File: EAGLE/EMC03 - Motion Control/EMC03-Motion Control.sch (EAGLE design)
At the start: 255 parts, among them J1 UART0, J10 S4B-PH-SM4, J11 S4B-PH-SM4, J12 S4B-PH-SM4, J13 S5B-PH-SM4, J14 S5B-PH-SM4, J15 S5B-PH-SM4, J16 S8B-PH-SM4, J17 S8B-PH-SM4, J18 S6B-PH-SM4, J19 S6B-PH-SM4, J2 FTSH-105-1-L-DV, J20 Intel EDISON, J21 PWRBUTTON, J22 SERIAL CONS., J23 B14B-PH, J3 USB-A, J4 101-00581-59, J5 S3B-PH-SM4, J6 S3B-PH-SM4, J7 S3B-PH-SM4, J8 694106106102, J9 ESTOP, Q1 12MHz, Q2 25MHz, U1 LPC1768, U10 FT231XS-R, U11 74LVC1T45, U12 74LVC1T45, U13 74LVC1T45, U14 74LVC1T45, U15 74LVC1T45, U16 TXS0206-29, U17 74LVC, U18 MIC2026-1YM, U19 MIC2026-1YM, U2 SP3485, U20 74LVC, U21 74LVC1T45, U22 74LVC1T45, U3 93LC66A, U4 LAN9514, U5 74AHCT, U6 TMC2130-LA, U7 TMC2130-LA, U8 TMC2130-LA, U9 SP3485

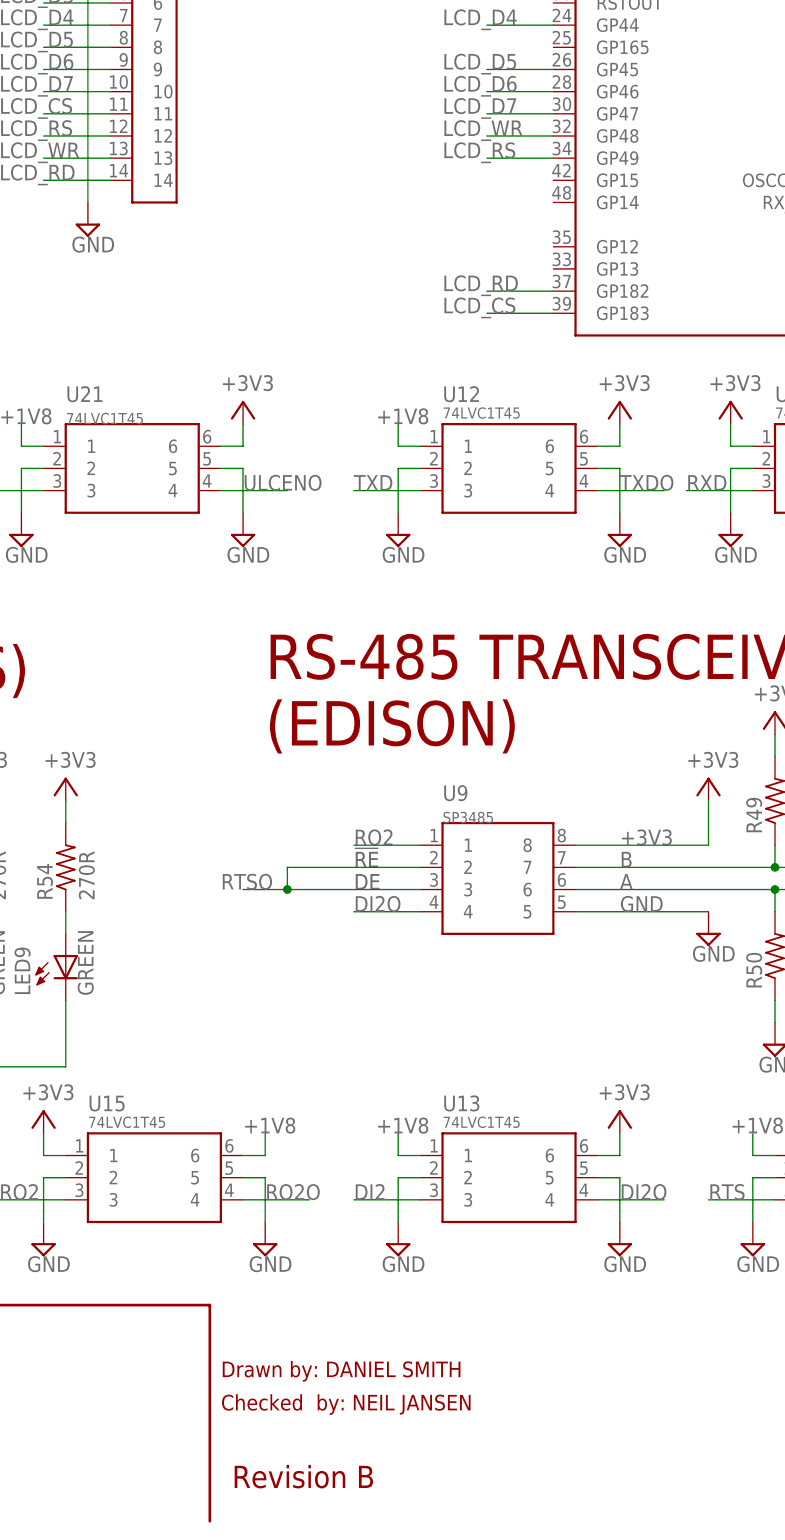
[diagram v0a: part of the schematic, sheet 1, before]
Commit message: Preliminary placement and routing done for EFD01. Preliminary placement done for EMC03. All schematics are ready for review (A0 for ECAM03 needs to be defined, also SS for EFD01, ECAM03, etc.)
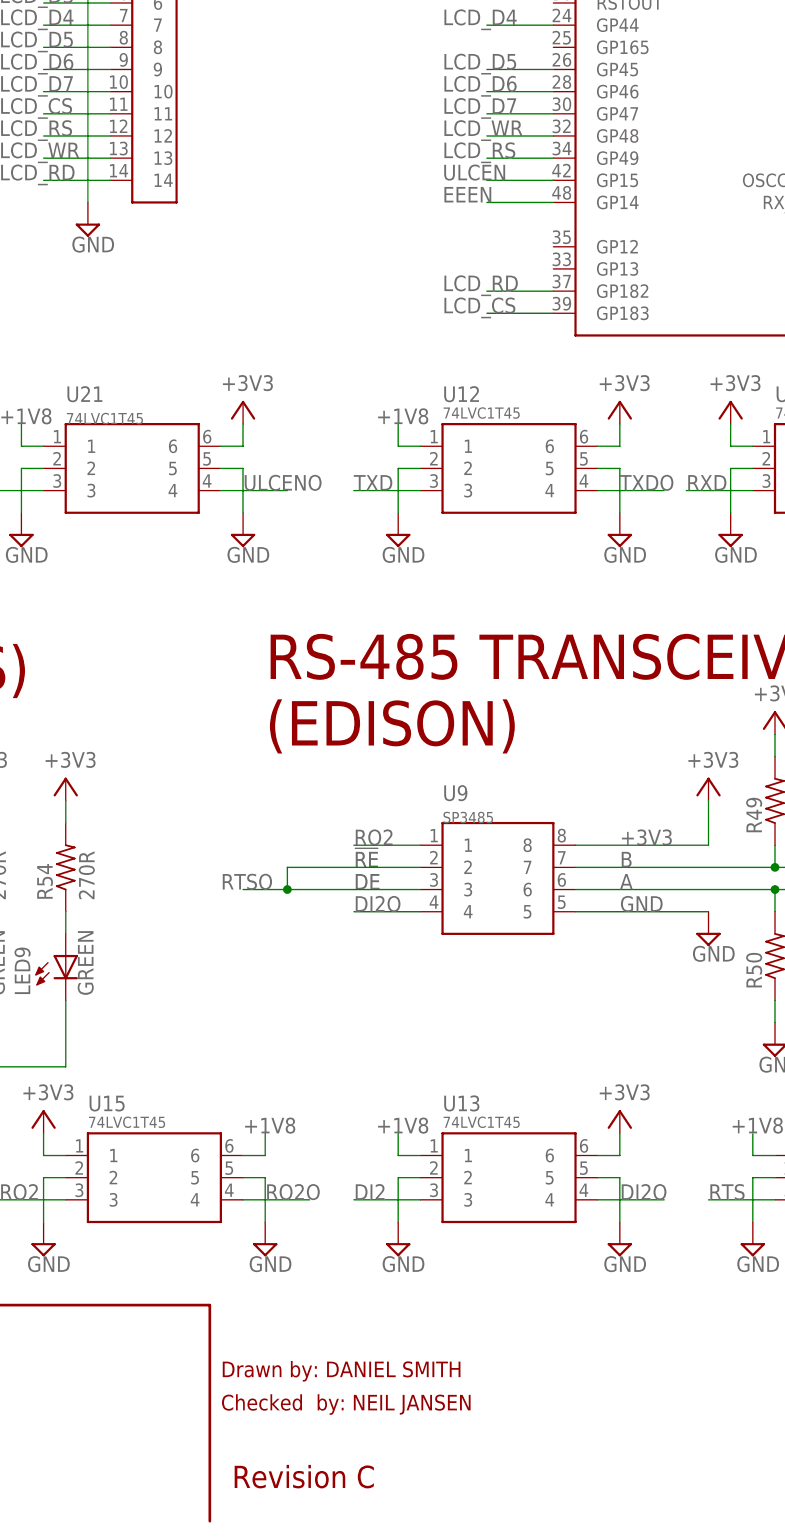
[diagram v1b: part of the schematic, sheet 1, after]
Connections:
- net EEEN: now also J20.GP14
- net ULCEN: now also J20.GP15
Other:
- note added: "Revision C"
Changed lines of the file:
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@@
 <text x="289.56" y="20.32" size="1.778" layer="94" ratio="15">Drawn by: DANIEL SMITH</text>
 <text x="289.56" y="16.51" size="1.778" layer="94" ratio="15">Checked  by: NEIL JANSEN</text>
-<text x="290.83" y="7.62" size="2.54" layer="94" ratio="10">Revision B</text>
+<text x="290.83" y="7.62" size="2.54" layer="94" ratio="10">Revision C</text>
 <wire x1="5.715" y1="28.575" x2="288.29" y2="28.575" width="0.3048" layer="94"/>
 <wire x1="288.29" y1="28.575" x2="288.29" y2="3.81" width="0.3048" layer="94"/>
@@
 <label x="256.54" y="121.92" size="1.778" layer="95"/>
 </segment>
+<segment>
+<pinref part="J20" gate="G$1" pin="GP15"/>
+<wire x1="327.66" y1="157.48" x2="320.04" y2="157.48" width="0.1524" layer="91"/>
+<label x="314.96" y="157.48" size="1.778" layer="95"/>
+</segment>
 </net>
 <net name="EEENO" class="0">
@@
 <label x="210.82" y="121.92" size="1.778" layer="95"/>
 </segment>
-</net>
+<segment>
+<pinref part="J20" gate="G$1" pin="GP14"/>
+<wire x1="327.66" y1="154.94" x2="320.04" y2="154.94" width="0.1524" layer="91"/>
+<label x="314.96" y="154.94" size="1.778" layer="95"/>
+</segment>
+</net>

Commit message: Split the EMC03 into EMC03 and EFP01 (front panel board) to make routing 10000000x easier
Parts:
- removed C13, C14, C18, C19, C20, C21, C22, C23, C33, C34, C35, C60, C74, C79, C80, C81, C82, C84, C85: 0.1uF, TinWhiskers:CPL-CAP-X5R-0603-0.1UF-35V
- removed C24, C25, C77: 0.1uF, TinWhiskers:CPL-CAP-X7R-0603-0.1UF-35V
- removed C26, C30, C31, C32: 18pF, TinWhiskers:CPL-CAP-C0G-0603-18PF-50V
- removed C3: 100uF, rcl:CPOL-USD
- removed C37: 220uF, TinWhiskers:CPL-CAP-ALU-SMD-220-50V
- removed C38: 470uF, TinWhiskers:CPL-CAP-ALU-SMD-470UF-25V
- removed C4: 0.1uF, TinWhiskers:CPL-CAP-X7R-0603-100NF-50V
- removed C61, C83: 4.7uF, TinWhiskers:CPL-CAP-X5R-0603-4.7UF-10V
- removed C73: 1.0uF, TinWhiskers:CPL-CAP-X5R-0603-1UF-50V
- removed C76: 0.47uF, TinWhiskers:CPL-CAP-X7R-0603-0.47UF-10V
- removed C78: 10nF, TinWhiskers:CPL-CAP-X7R-10NF-16V
- removed D2: SJPB-H6, TinWhiskers:CPL-DIO-SJPB-H6-SM2
- removed FB1, FB3, FB4: 120R, TinWhiskers:CPL-IND-FER-120OHM-2A
- removed FID1, FID2, FID3, FID4, FID5, FID6, FID7: FIDUCIAL, FirePick:FIDUCIAL
- removed J20: Intel EDISON, TinWhiskers:CPL-SBC-INTEL-EDISON
- removed J21: PWRBUTTON, TinWhiskers:CPL-CON-HEADER-0.1IN-2P-M
- removed J22: SERIAL CONS., TinWhiskers:CPL-CON-HEADER-0.1IN-4P-M
- removed J23: B14B-PH, TinWhiskers:CPL-CON-JST-2.0MM-14P-M-VRT
- removed J8: 694106106102, TinWhiskers:CPL-CON-BARREL-2.1MM-24V
- removed L1: 100uH, TinWhiskers:CPL-IND-100UH-1.8A
- removed LED10, LED11, LED12, LED13, LED14, LED8, LED9: GREEN, TinWhiskers:CPL-LED-0603-GREEN
- removed LED6, LED7: RED, TinWhiskers:CPL-LED-0603-RED
- removed LOGO4: LOGO-FIREPICKLARGE, FirePick:LOGO-FIREPICKLARGE
- removed LOGO5: LOGO-OSHWMEDIUM, FirePick:LOGO-OSHWMEDIUM
- removed LOGO6: LOGO-CC-BY-SALARGE, FirePick:LOGO-CC-BY-SALARGE
- removed Q2: 25MHz, TinWhiskers:CPL-OSC-CRY-25MHZ-18PF
- removed R11: 1M, TinWhiskers:CPL-RES-0603-1M-0.1W
- removed R12: 825R, TinWhiskers:CPL-RES-0603-825-0.1W
- removed R13: 12.4K, TinWhiskers:CPL-RES-0603-12.4K-0.1W
- removed R14, R43, R48: 10K, TinWhiskers:CPL-RES-0603-10K-0.1W
- removed R15, R57: 0R1, TinWhiskers:CPL-RES-0603-0.1-0.1W
- removed R16, R58: DNP, TinWhiskers:CPL-RES-0603-0-0.1W
- removed R17, R23: 10.5K, TinWhiskers:CPL-RES-0603-10.5K-0.1W
- removed R22, R30, R31, R32: 49R9, TinWhiskers:CPL-RES-0603-49.9-0.1W
- removed R33, R34: 330R, TinWhiskers:CPL-RES-0603-330-0.1W
- removed R35: 12K, TinWhiskers:CPL-RES-0603-12K-0.1W
- removed R36: 0R, TinWhiskers:CPL-RES-0603-0-0.1W
- removed R37, R52, R55, R56: 511R, TinWhiskers:CPL-RES-0603-511-0.1W
- removed R42: 1.2K, TinWhiskers:CPL-RES-0603-1.2K-0.1W
- removed R49, R50: 1K, TinWhiskers:CPL-RES-0603-1K-0.1W
- removed R51: 120R, TinWhiskers:CPL-RES-0603-120-0.1W
- removed R53, R54: 270R, TinWhiskers:CPL-RES-0603-270-0.1W
- removed RJ1: HR911105A, TinWhiskers:CPL-ETH-MACJACK-LED-SHLD
- removed TP2: +5V, TinWhiskers:TPAD
- removed U$25: TIN-WHISKERSTSTOP, !tin-whiskers:TIN-WHISKERSTSTOP
- removed U10: FT231XS-R, TinWhiskers:CPL-USB-FT2321XS
- removed U11, U12, U13, U14, U15, U21, U22: 74LVC1T45, TinWhiskers:CPL-TRS-74LVC1T45
- removed U16: TXS0206-29, TinWhiskers:TXS0206-29
- removed U17, U20: 74LVC, TinWhiskers:CPL-IC-LOGIC-OR-1CH-74LVC
- removed U18, U19: MIC2026-1YM, TinWhiskers:CPL-PWR-SWI-2CH-MIC2026-1XX
- removed U3: 93LC66A, TinWhiskers:CPL-MEM-512KB-EEPROM-SOT23-6
- removed U4: LAN9514, TinWhiskers:CPL-USB-HUB-LAN9514
- removed U9: SP3485, TinWhiskers:SP3485
- removed VR1: SI-8050JD, TinWhiskers:CPL-REG-SWI-5V-1.5A
- C11: value 33pF -> 4.7 uF; device TinWhiskers:CPL-CAP-C0G-0603-33PF-50V -> TinWhiskers:CPL-CAP-X7R-0603-100NF-100V; PARTNO C0603C330K5GACTU -> UMK107B7104KA-T
- C12: value 33pF -> 4.7uF; device TinWhiskers:CPL-CAP-C0G-0603-33PF-50V -> TinWhiskers:CPL-CAP-X7R-0603-100NF-100V; PARTNO C0603C330K5GACTU -> UMK107B7104KA-T
- J3: value USB-A -> CONN-OSTTH050160; device TinWhiskers:CPL-CON-HEADER-0.1IN-4P-M -> FirePick:CONN-OSTTH050160; PARTNO 68000-104HLF -> (none)
- J4: value 101-00581-59 -> (none); device TinWhiskers:CPL-CON-MICSROSD(SD)-CD -> !con-lstb:MA07-2; PARTNO 101-00581-59 -> (none)
- R10: value 330R -> 2.2; device TinWhiskers:CPL-RES-0603-330-0.1W -> TinWhiskers:CPL-RES-1206-0.22-0.5W; PARTNO RC0603FR-07330RL -> RL1206FR-7W0R22L
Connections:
- removed net !DTR: U10.!DTR
- removed net !PWRBTN: J20.PWRBTN#, J21.1, R48.1
- removed net !RESET: R36.1
- removed net !RXLED: LED9.C
- removed net !TXLED: LED8.C
- removed net +1V8: C35.2, R17.2, R23.2, R57.1, R58.1, U11.6, U12.1, U13.1, U14.1, U15.6, U16.VCCA, U21.1, U22.1
- removed net CLKA: J20.GP78, U16.CLKA
- removed net CLKB: J4.CLK, U16.CLKB
- removed net CLKF: J20.GP84, U16.CLKF
- removed net CMD: J4.CMD
- removed net CMDA: J20.GP79, U16.CMDA
- removed net CMDB: U16.CMDB
- removed net DAT0A: J20.GP80, U16.DAT0A
- removed net DAT0B: J4.DAT0, U16.DAT0B
- removed net DAT1A: J20.GP81, U16.DAT1A
- removed net DAT1B: J4.DAT1, U16.DAT1B
- removed net DAT2: J4.DAT2
- removed net DAT2A: J20.GP82, U16.DAT2A
- removed net DAT2B: U16.DAT2B
- removed net DAT3: J4.CD/DAT3
- removed net DAT3A: J20.GP83, U16.DAT3A
- removed net DAT3B: U16.DAT3B
- removed net DI2: J20.GP131, U13.3
- removed net DI2O: U13.4, U9.4
- removed net DM: J22.3
- removed net DP: J22.2
- removed net EECLK: U3.CLK, U4.EECLK
- removed net EECS: U3.CS, U4.EECS
- removed net EEDI: U3.DO, U4.EEDI
- removed net EEDO: U3.DI, U4.EEDO
- removed net EEEN: J20.GP14, U22.3
- removed net EEENO: U17.A, U22.4
- removed net EN: R17.1, U16.EN
- removed net EXRES: R13.2, U4.EXRES
- removed net LCD_CS: J20.GP183, J23.11
- removed net LCD_D0: J20.GP40, J23.3
- removed net LCD_D1: J20.GP41, J23.4
- removed net LCD_D2: J20.GP42, J23.5
- removed net LCD_D3: J20.GP43, J23.6
- removed net LCD_D4: J20.GP44, J23.7
- removed net LCD_D5: J20.GP45, J23.8
- removed net LCD_D6: J20.GP46, J23.9
- removed net LCD_D7: J20.GP47, J23.10
- removed net LCD_RD: J20.GP182, J23.14
- removed net LCD_RS: J20.GP49, J23.12
- removed net LCD_WR: J20.GP48, J23.13
- removed net LED_DUPLEX: LED11.C, U4.GPIO0
- removed net LED_SPEED: RJ1.LED_Y+, U4.GPIO2
- removed net LED_TXRX: RJ1.LED_G+, U4.GPIO1
- removed net N$10: LED7.A, R42.1
- removed net N$11: LED9.A, R54.1
- removed net N$12: LED6.A, R43.1
- removed net N$13: LED8.A, R53.1
- removed net N$14: D2.C, L1.1, VR1.2
- removed net N$15: R36.2, U4.NRESET
- removed net N$18: R14.1, U4.MDIX_EN
- removed net N$19: J20.1.8V, R57.2, R58.2
- removed net N$21: J20.DCIN, J20.VSYS@2, J20.VSYS@4, J20.VSYS@6, R15.1, R16.1
- removed net N$22: U17.Y, U18.ENA
- removed net N$27: R35.2, U4.USBRBIAS
- removed net N$28: LED10.A, R37.1
- removed net N$29: LED12.A, R52.1
- removed net N$3: LED11.A, R10.1
- removed net N$30: LED13.A, R55.1
- removed net N$31: LED14.A, R56.1
- removed net N$4: C76.2, VR1.5
- removed net N$42: U18.ENB, U20.Y
- removed net N$6: R12.1, U4.VBUS_DET
- removed net N$7: R33.1, RJ1.LED_Y-
- removed net N$8: R34.1, RJ1.LED_G-
- removed net PRTCTL2: U17.B, U18.FLGA, U4.PRTCTL2
- removed net PRTCTL3: U18.FLGB, U20.B, U4.PRTCTL3
- removed net PRTCTL4: U19.ENA, U19.FLGA, U4.PRTCTL4
- removed net PRTCTL5: U19.ENB, U19.FLGB, U4.PRTCTL5
- removed net PWR3: J3.1, R52.2, U19.OUTA
- removed net PWR4: R37.2, U19.OUTB
- removed net RD+: C31.2, R31.1, RJ1.RD+, U4.RXP
- removed net RD-: C32.2, R32.1, RJ1.RD-, U4.RXN
- removed net RO2: U15.3, U9.1
- removed net RO2O: J20.GP130, U15.4
- removed net RTS: J20.GP129, U14.3
- removed net RTSO: U14.4, U9.2, U9.3
- removed net RXD: U11.3
- removed net RXDO: J20.GP134, U11.4
- removed net SD_CD: J20.GP77, J4.CD, R23.1, U16.CD
- removed net TD+: C26.2, R22.1, RJ1.TD+, U4.TXP
- removed net TD-: C30.2, R30.1, RJ1.TD-, U4.TXN
- removed net TXD: J20.GP135, U12.3
- removed net TXDO: U12.4
- removed net ULCEN: J20.GP15, U21.3
- removed net ULCENO: U20.A, U21.4
- removed net USBA_D+: J3.3, U4.USBDP4
- removed net USBA_D-: J3.2, U4.USBDM4
- removed net USBDM0: J20.USB_DN, U4.USBDM0
- removed net USBDP0: J20.USB_DP, U4.USBDP0
- removed net VCCB: C34.2, J4.VDD, U16.VCCB
- removed net VDD18C: C83.2, C84.2, C85.2, U4.V18COR@15, U4.V18COR@38
- removed net VDD18ETH: C74.2, FB4.2, U4.VDD18ETHPLL
- removed net VDD18USB: C73.2, FB4.1, U4.VDD18USBPLL
- removed net VDD33A: C13.2, C14.2, C18.2, C19.2, C20.2, C21.2, C22.2, FB1.1, U4.VDD33A@10, U4.VDD33A@49, U4.VDD33A@5, U4.VDD33A@51, U4.VDD33A@54, U4.VDD33A@57, U4.VDD33A@64
- removed net XI: C12.2, Q2.2, R11.2, U4.XI
- removed net XO: C11.2, Q2.1, R11.1, U4.XO
- net +24V: no longer C37.POS, J8.2, R43.2, VR1.1
- net +3V3: no longer C23.2, C24.2, C25.2, C33.2, C60.2, C61.2, C79.2, C80.2, C81.2, C82.2, FB1.2, FB3.2, J23.1, R10.2, R12.2, R14.2, R15.2, R16.2, R22.2, R30.2, R31.2, R32.2, R48.2, R49.2, R53.2, R54.2, RJ1.4, RJ1.5, U11.1, U12.6, U13.6, U14.6, U15.1, U16.VBATT, U17.VCC, U20.VCC, U21.6, U22.6, U3.VCC, U4.TEST3, U4.VDD33IO@19, U4.VDD33IO@27, U4.VDD33IO@33, U4.VDD33IO@39, U4.VDD33IO@46, U9.8
- net +5V: now also J4.1, J4.2; no longer C3.+, C38.POS, C4.1, L1.2, R42.2, TP2.2, U18.IN, U19.IN, U6.VCC, U6.VCC_IO, VR1.4
- net A: now also J4.14; no longer R50.2, R51.1, U9.6
- net B: now also J4.12; no longer R49.1, R51.2, U9.7
- net EE_D+: now also J4.13; no longer U4.USBDP3
- net EE_D-: now also J4.11; no longer U4.USBDM3
- net ESTOP: now also J4.4
- net GND: now also J4.10, J4.3, J4.9; no longer C13.1, C14.1, C18.1, C19.1, C20.1, C21.1, C22.1, C23.1, C24.1, C25.1, C26.1, C3.-, C30.1, C31.1, C32.1, C33.1, C34.1, C35.1, C37.NEG, C38.NEG, C4.2, C60.1, C61.1, C73.1, C74.1, C76.1, C77.1, C78.1, C79.1, C80.1, C81.1, C82.1, C83.1, C84.1, C85.1, D2.A, J20.GND@1, J20.GND@11, J20.GND@13, J20.GND@15, J20.GND@5, J20.GND@9, J21.2, J22.4, J23.2, J3.4, J4.GND, J4.GND2, J4.NC, J4.VSS, LED10.C, LED12.C, LED13.C, LED14.C, LED6.C, LED7.C, R13.1, R33.2, R34.2, R35.1, R50.1, RJ1.SHLD0, RJ1.SHLD1, U11.2, U11.5, U12.2, U12.5, U13.2, U13.5, U14.2, U14.5, U15.2, U15.5, U16.GND@C2, U16.GND@C3, U17.GND, U18.GND, U19.GND, U20.GND, U21.2, U21.5, U22.2, U22.5, U3.VSS, U4.CLK24_EN, U4.PAD, U4.TEST2, U9.5, VR1.3, VR1.GND
- net N$1: now also C11.2, R10.2, U6.VCC, U6.VCC_IO; no longer C77.2
- net N$2: now also C12.2, R10.1, U6.5VOUT; no longer C78.2, FB3.1, J22.1
- net PWR1: no longer R56.2, U18.OUTA
- net PWR2: no longer R55.2, U18.OUTB
- net ULC_D+: now also J4.7; no longer U4.USBDP2
- net ULC_D-: now also J4.5; no longer U4.USBDM2
- net USBMCU+: now also J4.8; no longer U4.USBDP5
- net USBMCU-: now also J4.6; no longer U4.USBDM5
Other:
- note added: "Connector should be mounted on under-side of board, and point down Connector should be through-hole"
- note added: "TODO: 100 uF"
- note added: "TODO: 100 uF caps on each"
- note added: "TODO: REMOVE J9 AND WIRE E-STOP PIN/NET TO ~11-PIN CONNECTOR"
- note added: "todo: add power connector (probably a screw terminal, exact type that we're using on emc02) (on-shore technology -- look at old bom / SCH)"
- note added: "todo: change C50 to 6.3mm can size"
- note added: "todo: make a smaller inductor, it needs less current now....."
- note added: "todo: make these 5vout like the first one"
- note added: "todo: un-neil the connector"
- note removed: "(EDISON)"
- note removed: "*Review values for these 18pF caps."
- note removed: "EEPROM"
- note removed: "ETHERNET INTERFACE"
- note removed: "INTEL EDISON"
- note removed: "MICRO SD INTERFACE"
- note removed: "POWER"
- note removed: "PWR BUTTON"
- note removed: "SERIAL CONSOLE"
- note removed: "USB HUB CHIP"
- note removed: "USB-A"
- note removed: "USB-A CHIP (S CONS)"
- note removed: "VSS"

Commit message: Finalized schematics (minus potential LDO regulator) for all boards. Layout partially done for EFD01
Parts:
- removed C36: 220uF, TinWhiskers:CPL-CAP-ALU-SMD-220-50V
- removed C50: 470uF, TinWhiskers:CPL-CAP-ALU-SMD-470UF-25V
- removed D1: 1N4148, SparkFun-DiscreteSemi:DIODESOD123
- removed J16: S8B-PH-SM4, TinWhiskers:CPL-CON-JST-2.0MM-8P-M-RA
- removed J18: S6B-PH-SM4, TinWhiskers:CPL-CON-JST-2.0MM-6P-M-RA
- removed J3: CONN-OSTTH050160, FirePick:CONN-OSTTH050160
- removed J4: (no value), !con-lstb:MA07-2
- removed J9: ESTOP, TinWhiskers:CPL-CON-HEADER-0.1IN-2P-M
- removed L2: 100uH, TinWhiskers:CPL-IND-100UH-1.8A
- removed LOGO11: LOGO-FIREPICKLARGE, FirePick:LOGO-FIREPICKLARGE
- removed LOGO2: LOGO-OSHWMEDIUM, FirePick:LOGO-OSHWMEDIUM
- removed LOGO3, LOGO7, LOGO9: LOGO-CC-BY-SALARGE, FirePick:LOGO-CC-BY-SALARGE
- removed R27: 100K, TinWhiskers:CPL-RES-0603-100K-0.1W
- removed R28: 10K, TinWhiskers:CPL-RES-0603-10K-0.1W
- removed R29: 4.7K, TinWhiskers:CPL-RES-0603-4.7K-0.1W
- removed U5: 74AHCT, TinWhiskers:CPL-IIC-BUF-74AHCT-SC70
- added C13, C14, C18, C19: 4.7uF, TinWhiskers:CPL-CAP-X5R-0603-4.7UF-10V
- added C20, C21, C22: 100uF, TinWhiskers:CPL-CAP-ALU-SMD-100UF-50V
- added C3: 220uF, TinWhiskers:CPL-CAP-ALU-SMD-220UF-16V
- added C4: 470uF, TinWhiskers:CPL-CAP-ALU-SMD-470UF-10V
- added L1: 100uH, TinWhiskers:CPL-IND-100UH-700MA-2020
- added R11, R12: 2R2, TinWhiskers:CPL-RES-0603-2.2-0.1W
- added TB1: DC-IN, TinWhiskers:CPL-TBLK-SCR-3CKT-5.0MM-OST
- added U3: 74LVC, TinWhiskers:CPL-IC-LOGIC-OR-1CH-74LVC
- C11: value 4.7 uF -> 4.7uF; device TinWhiskers:CPL-CAP-X7R-0603-100NF-100V -> TinWhiskers:CPL-CAP-X5R-0603-4.7UF-10V; PARTNO UMK107B7104KA-T -> (none)
- C12: device TinWhiskers:CPL-CAP-X7R-0603-100NF-100V -> TinWhiskers:CPL-CAP-X5R-0603-4.7UF-10V; PARTNO UMK107B7104KA-T -> (none)
- C16, C40, C63: value 470 nF -> 470nF
- C17, C41, C42, C52, C64, C65: value 100 nF -> 100nF
- R10: value 2.2 -> 2R2; device TinWhiskers:CPL-RES-1206-0.22-0.5W -> TinWhiskers:CPL-RES-0603-2.2-0.1W; PARTNO RL1206FR-7W0R22L -> (none)
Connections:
- removed net !ENABLE_BUF: U1.P1-24, U5.A
- removed net EE_D+: J16.7, J4.13
- removed net EE_D-: J16.8, J4.11
- removed net ESTOP_OE: D1.A, J9.2, R27.1, U5.OE
- removed net PWR1: J16.6
- removed net PWR2: J17.6
- removed net ULC_D+: J17.7, J4.7
- removed net ULC_D-: J17.8, J4.5
- new net !ENABLE_LPC: U1.P1-24, U3.B
- new net !ENABLE_MOD: J17.2, J19.2, U3.A
- new net N$3: C19.2, R11.1, U8.5VOUT
- new net N$4: C18.2, R11.2, U8.VCC, U8.VCC_IO
- new net N$6: C13.2, R12.2, U7.VCC, U7.VCC_IO
- net !ENABLE: now also U3.Y; no longer J16.2, J17.2, J18.2, J19.2, R28.1, U5.Y
- net +24V: now also C20.POS, C21.POS, C22.POS, TB1.1; no longer J16.1, J18.1
- net +3V3: now also C4.POS, L1.2, U3.VCC; no longer C50.POS, L2.2, R27.2, R28.2, U5.VCC
- net +5V: now also C3.POS, J17.6, TB1.2; no longer C36.POS, J18.6, J4.1, J4.2, U7.VCC, U7.VCC_IO, U8.VCC, U8.VCC_IO
- net A: no longer J16.4, J18.4, J4.14
- net B: no longer J16.5, J18.5, J4.12
- net ESTOP: no longer D1.C, J4.4
- net GND: now also C13.1, C14.1, C18.1, C19.1, C20.NEG, C21.NEG, C22.NEG, C3.NEG, C4.NEG, TB1.3, U3.GND; no longer C36.NEG, C50.NEG, J16.3, J18.3, J4.10, J4.3, J4.9, R29.1, U5.GND
- net N$16: now also L1.1; no longer L2.1
- net N$5: now also C14.2, R12.1, U7.5VOUT; no longer J9.1, R29.2
- net USBMCU+: now also J17.7; no longer J4.8
- net USBMCU-: now also J17.8; no longer J4.6
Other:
- note added: "IC PWR"
- note added: "TEST PADS"
- note added: "TOOL"
- note added: "VOLTAGE REG"
- note removed: "!EN! BUFFERING"
- note removed: "* Add digital potentiometer adjustment circuit for DRV8825's"
- note removed: "* Replace BSS138's on I2C bus with PCA9512? (hot swap protection)"
- note removed: "* Replace StepSticks with DRV8825's"
- note removed: "**TODO:"
- note removed: "1A Schottky Diodes like MSS1P6 or MSS1P3 (VM limited to 30V)"
- note removed: "CAMERA"
- note removed: "Change to SMD pads, bottom"
- note removed: "Connector should be mounted on under-side of board, and point down Connector should be through-hole"
- note removed: "E-STOP"
- note removed: "EFFECTOR"
- note removed: "EMERGENCY STOP SWITCH (NORMALLY CLOSED TYPE) USE JUMPER IF NOT PRESENT"
- note removed: "END"
- note removed: "LOGIC IC PWR"
- note removed: "NOTE: ACTIVE LOW"
- note removed: "Released under the Creative Commons Attribution Share-Alike 4.0 License"
- note removed: "Revision --: First dev release"
- note removed: "Revision A: Arduino Due support added"
- note removed: "Revision B: Added R36,R45,C7. Unconnected Arduino VIN to +12V. Fixed PCB routing issue. Moved TOOL4_DOUT_BUF and !TOOL4_EN_BUF! from 18/19 to"
- note removed: "TEST POINTS"
- note removed: "TODO: 100 uF"
- note removed: "TODO: 100 uF caps on each"
- note removed: "TODO: INSTALL FERRITE BEAD ON ISENSE?"
- note removed: "TODO: REMOVE J9 AND WIRE E-STOP PIN/NET TO ~11-PIN CONNECTOR"
- note removed: "TOOL1"
- note removed: "TOOL2"
- note removed: "UP-LOOK"
- note removed: "todo: add power connector (probably a screw terminal, exact type that we're using on emc02) (on-shore technology -- look at old bom / SCH)"
- note removed: "todo: change C50 to 6.3mm can size"
- note removed: "todo: make a smaller inductor, it needs less current now....."
- note removed: "todo: make these 5vout like the first one"
- note removed: "todo: un-neil the connector"

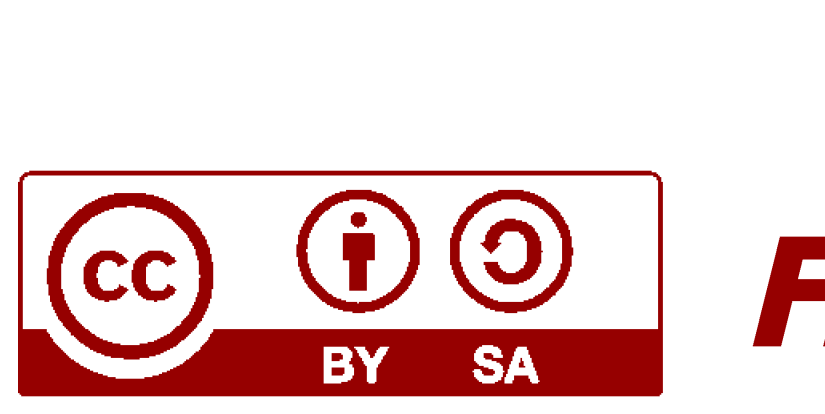
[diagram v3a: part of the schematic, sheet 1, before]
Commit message: Replaced switching regulator with a smaller LDO, with smaller accompanying components. Preliminary component placement for EMC03. Partial routing of power nets.
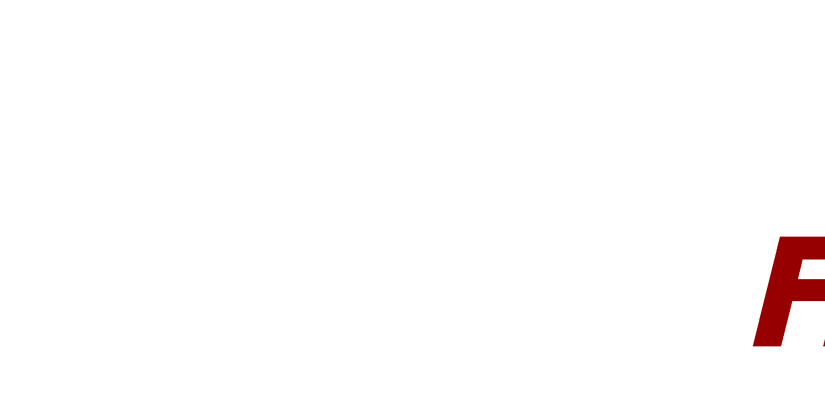
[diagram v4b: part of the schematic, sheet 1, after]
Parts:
- removed C51: 0.47uF, TinWhiskers:CPL-CAP-X7R-0603-0.47UF-10V
- removed D15: SJPB-H6, TinWhiskers:CPL-DIO-SJPB-H6-SM2
- removed L1: 100uH, TinWhiskers:CPL-IND-100UH-700MA-2020
- removed LOGO8: LOGO-CC-BY-SALARGE, FirePick:LOGO-CC-BY-SALARGE
- removed VR2: SI-8033JD, TinWhiskers:CPL-REG-SWI-3.3V-1.5A
- added VR1: LMS8117AMP-3.3/NOPB, TinWhiskers:CPL-REG-LIN-3.3V-1A
- C3: value 220uF -> 10uF; device TinWhiskers:CPL-CAP-ALU-SMD-220UF-16V -> TinWhiskers:CPL-CAP-ALU-6.4MM-10UF-10V
- C4: value 470uF -> 10uF; device TinWhiskers:CPL-CAP-ALU-SMD-470UF-10V -> TinWhiskers:CPL-CAP-ALU-6.4MM-10UF-10V
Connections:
- removed net N$16: D15.C, L1.1, VR2.2
- removed net N$17: C51.2, VR2.5
- net +3V3: now also VR1.OUT; no longer L1.2, VR2.4
- net +5V: now also VR1.IN; no longer VR2.1
- net GND: now also VR1.GND, VR1.TAB; no longer C51.1, D15.A, VR2.3, VR2.GND
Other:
- note removed: "* 5V Switching Regulator: Powers LEDs, Endstops"
- moved on the sheet: C3, C4
